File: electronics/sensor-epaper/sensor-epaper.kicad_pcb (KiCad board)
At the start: 4 copper layers, 34 x 68 mm, 74 parts, among them J1 i2c, J2 SWD, J4 Display, Q1 Q_NMOS_GSD, Q2 NX2301P, U2 ATSAMD21G18A-A, U3 AP3012, Y1 32.768

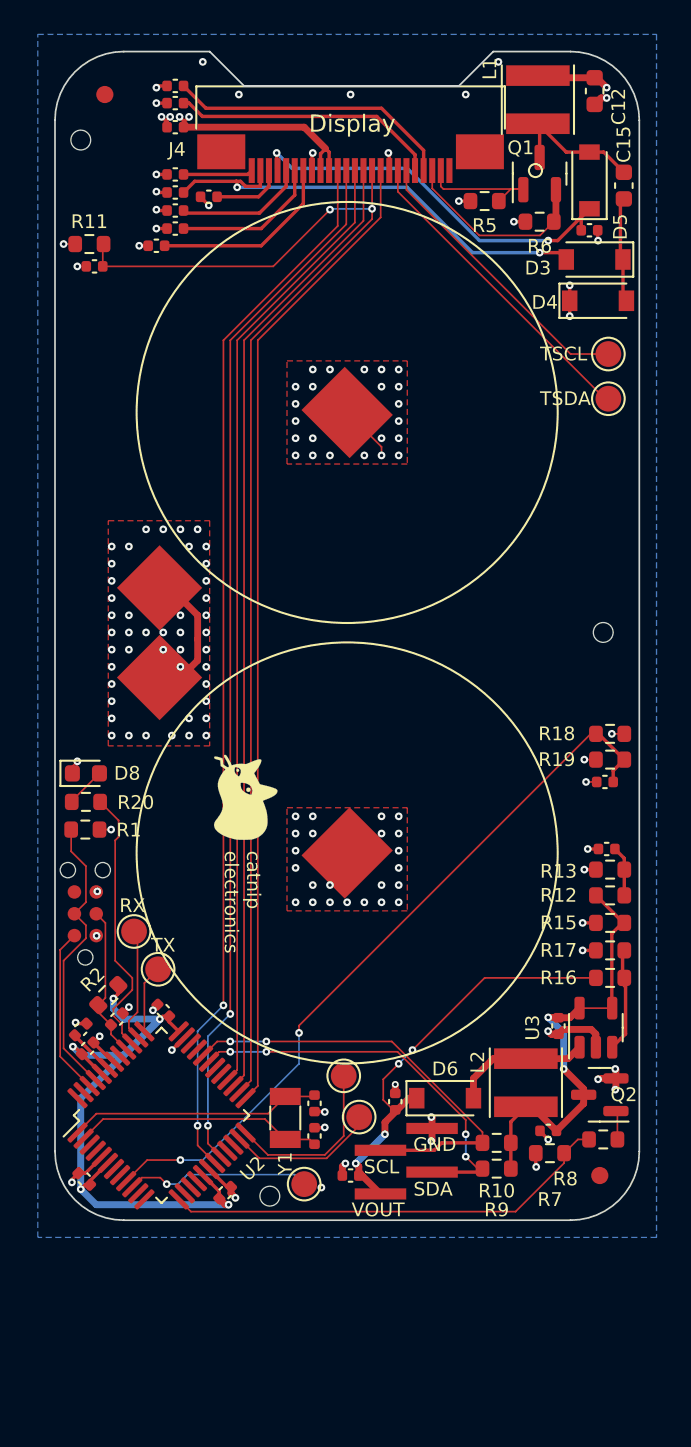
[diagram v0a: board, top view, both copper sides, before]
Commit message: Implement fixes for v1.0.0 board: * Fixed mirrored display connector * Fixed wrong button pinout * Remove CS from GPIO11 which is VDD_SPI after all, add a requisite cap * Add tantallum bulk cap, add more capacitance near MCU to counter power gulp related resets using thin USB cable * Consolidate some passive values
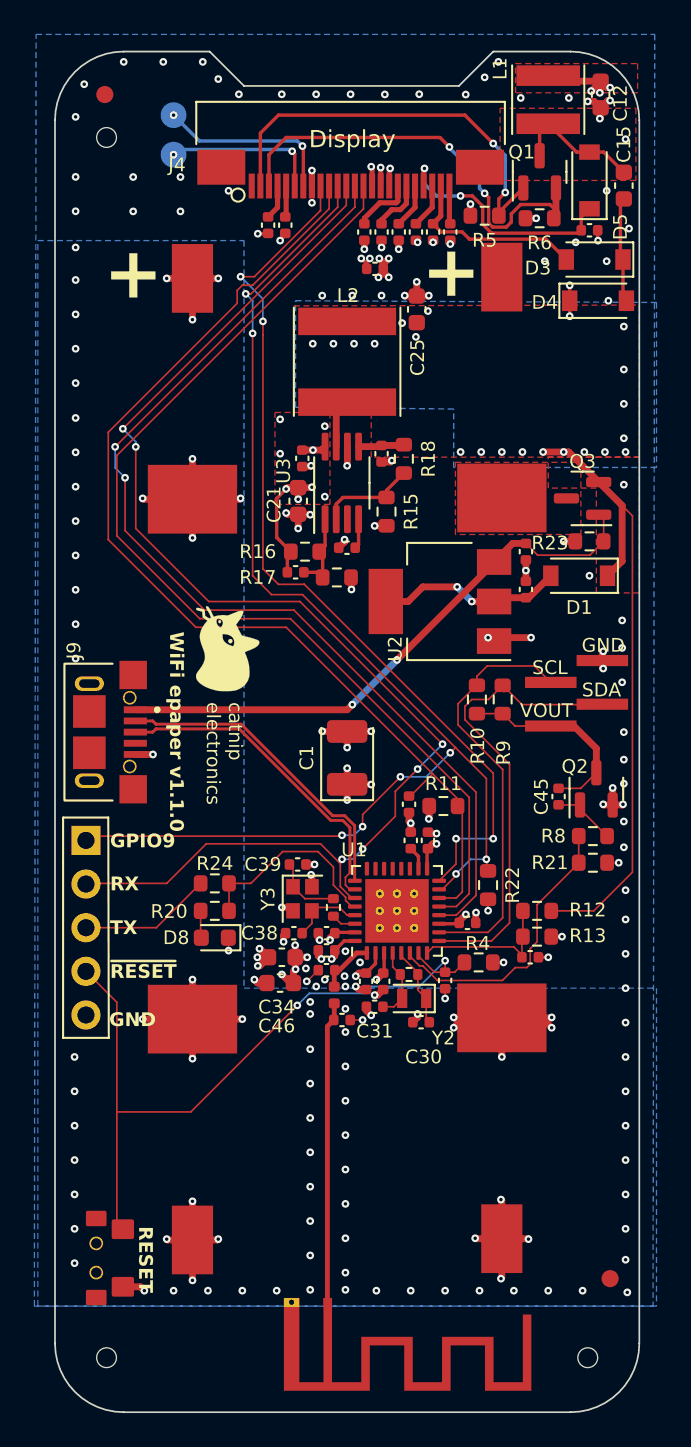
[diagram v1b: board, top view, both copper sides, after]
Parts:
- removed C19, C20, C3, C4, C5, C6: 1u, Capacitor_SMD:C_0402_1005Metric
- removed C2: 22p, Capacitor_SMD:C_0402_1005Metric
- removed D6: MBR0530, Diode_SMD:D_SOD-123
- removed the H6 at (178.5, 103.6)
- removed the H6 at (197.9, 70.8)
- removed R1, R2: 1k, Resistor_SMD:R_0603_1608Metric
- removed R19, R7: 1M, Resistor_SMD:R_0603_1608Metric
- removed TP1, TP2, TP3, TP4, TP5: TestPoint, TestPoint:TestPoint_Pad_D1.5mm
- removed Y1: 32.768, Crystal:Crystal_SMD_3215-2Pin_3.2x1.5mm
- added AE1: PCB Antenna, miceuz-lib:Texas_SWRA117D_2.4GHz_Left, F.Cu at (181.9, 109.8)
- added C28: 1u, Capacitor_SMD:C_0402_1005Metric, F.Cu at (187.7, 82.9)
- added C29: 1u, Capacitor_SMD:C_0402_1005Metric, F.Cu at (181.8, 89.3)
- added C30: 18p, Capacitor_SMD:C_0402_1005Metric, F.Cu at (187.3, 93.5)
- added C31: 18p, Capacitor_SMD:C_0402_1005Metric, F.Cu at (184.6, 92.6)
- added C32: 1u, Capacitor_SMD:C_0402_1005Metric, F.Cu at (190.0, 87.7)
- added C33: 1u, Capacitor_SMD:C_0402_1005Metric, F.Cu at (184.1, 91.1)
- added C34: 22u, Capacitor_SMD:C_0603_1608Metric, F.Cu at (179.2, 89.7)
- added C35: 1u, Capacitor_SMD:C_0402_1005Metric, F.Cu at (188.7, 91.0)
- added C36: ?, Capacitor_SMD:C_0402_1005Metric, F.Cu at (181.8, 90.5)
- added C37: ?, Capacitor_SMD:C_0402_1005Metric, F.Cu at (182.7, 93.3)
- added C38: 12p, Capacitor_SMD:C_0402_1005Metric, F.Cu at (179.9, 88.3)
- added C39: 12p, Capacitor_SMD:C_0402_1005Metric, F.Cu at (180.1, 84.3)
- added C40: 1u, Capacitor_SMD:C_0402_1005Metric, F.Cu at (185.1, 91.1)
- added C41: 1u, Capacitor_SMD:C_0402_1005Metric, F.Cu at (181.8, 88.3)
- added C42: 10p, Capacitor_SMD:C_0402_1005Metric, F.Cu at (180.0, 67.3)
- added C43: 1u, Capacitor_SMD:C_0402_1005Metric, F.Cu at (193.4, 66.1)
- added C44: 1u, Capacitor_SMD:C_0402_1005Metric, F.Cu at (193.4, 68.3)
- added C45: 1u, Capacitor_SMD:C_0402_1005Metric, F.Cu at (195.3, 80.3)
- added C46: 22u, Capacitor_SMD:C_0603_1608Metric, F.Cu at (179.1, 91.2)
- added C47: 1u, Capacitor_SMD:C_0402_1005Metric, F.Cu at (186.7, 82.9)
- added D1: 1N4148, Diode_SMD:D_SOD-123, F.Cu at (196.5, 67.5)
- added H6: ToolingHole, miceuz-lib:JLC_ToolingHole, F.Cu at (197.0, 113.0)
- added H6: ToolingHole, miceuz-lib:JLC_ToolingHole, F.Cu at (169.0, 113.0)
- added J9: USB micro, miceuz-lib:XKB_U254-051T-4BH83-F1S, F.Cu at (168.0, 76.6)
- added L3: 0, Inductor_SMD:L_0402_1005Metric, F.Cu at (182.2, 91.9)
- added Q3: NX2301P, Package_TO_SOT_SMD:SOT-23, F.Cu at (196.7, 63.0)
- added R14: 0, Resistor_SMD:R_0402_1005Metric, F.Cu at (182.2, 86.8)
- added R21: 1M, Resistor_SMD:R_0603_1608Metric, F.Cu at (197.3, 84.2)
- added R22: 1M, Resistor_SMD:R_0603_1608Metric, F.Cu at (191.2, 85.5)
- added R23: 4.7k, Resistor_SMD:R_0603_1608Metric, F.Cu at (197.1, 65.5)
- added R24: 150, Resistor_SMD:R_0603_1608Metric, F.Cu at (175.3, 85.4)
- added R3: ?, Resistor_SMD:R_0402_1005Metric, F.Cu at (186.6, 90.7)
- added R4: 4.7k, Resistor_SMD:R_0603_1608Metric, F.Cu at (190.7, 90.0)
- added SW1: SW_Push, miceuz-lib:SHOUHAN_TS24CA, F.Cu at (168.4, 107.2)
- added U1: ESP32-C3FN4, Package_DFN_QFN:QFN-32-1EP_5x5mm_P0.5mm_EP3.7x3.7mm_ThermalVias, F.Cu at (185.9, 87.0)
- added Y2: 32kHz, Crystal:Crystal_SMD_2012-2Pin_2.0x1.2mm, F.Cu at (186.9, 92.1)
- added Y3: 40MHz 10ppm, Crystal:Crystal_SMD_2016-4Pin_2.0x1.6mm, F.Cu at (180.4, 86.3)
- BT1, BT2: footprint miceuz-lib:2450_battery -> miceuz-lib:AA_KEYCO_53_SMD
- C1: value 22p -> 100u; footprint Capacitor_SMD:C_0402_1005Metric -> Capacitor_Tantalum_SMD:CP_EIA-3528-15_AVX-H
- C21, C25: value 1u -> 22u; footprint Capacitor_SMD:C_0402_1005Metric -> Capacitor_SMD:C_0603_1608Metric
- J2: value SWD -> Conn_01x06; footprint miceuz-lib:TC2030-MCP-NL -> Connector_PinHeader_2.54mm:PinHeader_1x05_P2.54mm_Vertical
- L2: footprint Inductor_SMD:L_Taiyo-Yuden_NR-40xx -> Inductor_SMD:L_Taiyo-Yuden_NR-60xx
- R11, R20: value 1k -> 4.7k
- R15: value 1k -> 300k
- R16: value 1k -> 348k
- R17: value 1k -> 200k
- R18: value 1M -> 220k
- R5: value 10k -> 4.7k
- TP6: value TSCL -> TestPoint; moved to B.Cu
- TP7: value TSDA -> TestPoint; moved to B.Cu
- U2: value ATSAMD21G18A-A -> AMS1117-3.3; footprint Package_QFP:TQFP-48_7x7mm_P0.5mm -> Package_TO_SOT_SMD:SOT-223-3_TabPin2
- U3: value AP3012 -> NCP1421; footprint Package_TO_SOT_SMD:SOT-23-5 -> Package_SO:MSOP-8_3x3mm_P0.65mm
- moved C25 48.4 mm to (187.1, 52.0), turned to 90 degrees
- moved L2 43.2 mm to (183.0, 55.0), turned to -90 degrees
- moved C22 41.8 mm to (180.4, 60.7), turned to -90 degrees
- moved R11 38.6 mm to (188.6, 80.9)
- moved C23 36.3 mm to (186.6, 80.8), turned to -90 degrees
- moved C21 35.4 mm to (180.2, 63.1), turned to -90 degrees
- moved U3 35.0 mm to (182.7, 62.1)
- moved C26 34.9 mm to (185.0, 60.4)
- moved U2 34.0 mm to (188.4, 69.0), turned to 0 degrees
- moved R16 30.5 mm to (180.6, 66.1)
- moved TP7 30.2 mm to (172.9, 40.7), turned to -90 degrees
- moved J1 29.0 mm to (196.3, 74.3)
- moved TP6 27.8 mm to (172.9, 43.0), turned to -90 degrees
- moved R9 27.3 mm to (192.1, 74.7), turned to 90 degrees
- moved R15 27.2 mm to (185.3, 63.8), turned to -90 degrees
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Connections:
- net Net-(D5-A) renamed /SW_NODE_DISPLAY
- net Net-(Q2-G) renamed /I2C-interface/I2C_EN_GATE
- BT1 pad 1: +BATT -> /MID_BATT
- BT2 pad 2: GND -> /MID_BATT
- C1 pad 1: Net-(U2-PA00) -> +3V3
- C12 pad 1: +BATT -> +3V3
- C21 pad 1: /I2C-interface/VOUT -> +3V3
- C22 pad 1: /I2C-interface/VOUT -> +3V3
- C24 pad 1: /I2C-interface/VIN_FEEDBACK -> /BATT_VOLTAGE
- C25 pad 1: Net-(Q2-D) -> /VIN
- C26 pad 1: Net-(Q2-D) -> /VIN
- C27 pad 1: /BATT_VOLTAGE -> /REF_MAIN
- C8 pad 1: +BATT -> +3V3
- J1 pad 1: /I2C-interface/VOUT -> /VI2C
- J2 pad 1: +BATT -> /D/C
- J2 pad 2: /SWD_IO -> /~{CS}
- J2 pad 3: /~{MCU_RST} -> Net-(J2-Pin_3)
- J2 pad 4: /SWD_CLK -> /CHIP_EN
- J4 pad 15: +BATT -> +3V3
- J4 pad 16: +BATT -> +3V3
- L1 pad 1: +BATT -> +3V3
- L2 pad 1: Net-(Q2-D) -> /VIN
- L2 pad 2: Net-(D6-A) -> /SW_MAIN
- Q2 pad 2: +BATT -> +3V3
- Q2 pad 3: Net-(Q2-D) -> /VI2C
- R10 pad 1: Net-(Q2-D) -> /VI2C
- R11 pad 1: +BATT -> +3V3
- R12 pad 1: Net-(Q2-D) -> /VIN
- R12 pad 2: /I2C-interface/VIN_FEEDBACK -> /BATT_VOLTAGE
- R13 pad 1: /I2C-interface/VIN_FEEDBACK -> /BATT_VOLTAGE
- R15 pad 1: Net-(Q2-D) -> /EN_MAIN
- R16 pad 1: /I2C-interface/VOUT -> +3V3
- R16 pad 2: Net-(U3-FB) -> /FB_MAIN
- R17 pad 1: Net-(U3-FB) -> /FB_MAIN
- R18 pad 1: +BATT -> /VIN
- R18 pad 2: /BATT_VOLTAGE -> /EN_MAIN
- R20 pad 2: Net-(U2-PA27) -> /TXD
- R9 pad 1: Net-(Q2-D) -> /VI2C
- U2 pad 1: Net-(U2-PA00) -> GND
- U2 pad 2: Net-(U2-PA01) -> /USB_3V3
- U2 pad 3: unconnected-(U2-PA02/A0) -> VBUS
- U3 pad 1: Net-(D6-A) -> /FB_MAIN
- U3 pad 2: GND -> /EN_MAIN
- U3 pad 3: Net-(U3-FB) -> (no net)
- U3 pad 4: Net-(Q2-D) -> /REF_MAIN
- U3 pad 5: Net-(Q2-D) -> /VIN
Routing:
- net +BATT: track 72.0 -> 0.00 mm, vias 66 -> 0
- net /CHIP_EN: track 0.00 -> 42.6 mm, vias 0 -> 2
- net /VIN: track 0.00 -> 42.0 mm, vias 0 -> 16
- net +3V3: track 0.00 -> 41.7 mm, vias 0 -> 37
- net /MID_BATT: track 0.00 -> 37.7 mm, vias 0 -> 16
- net /BATT_VOLTAGE: track 43.3 -> 8.50 mm, vias 2 -> 0
- net VBUS: track 0.00 -> 33.5 mm, vias 0 -> 2
- net Net-(Q2-D): track 25.9 -> 0.00 mm, vias 2 -> 0
- net GND: track 40.1 -> 65.9 mm, vias 88 -> 194
- net /I2C-interface/VOUT: track 25.0 -> 0.00 mm, vias 4 -> 0
- net /~{CS}: track 56.0 -> 76.7 mm, vias 0 -> 6
- net /D/C: track 56.4 -> 76.1 mm, vias 0 -> 8
- net /D+: track 0.00 -> 18.7 mm
- net /D-: track 0.00 -> 18.5 mm
- net /ANT_COMP: track 0.00 -> 17.5 mm
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- added copper zone on B.Cu, net +3V3
- added copper zone on F.Cu, net +3V3
- added copper zone on B.Cu, net /MID_BATT
- added copper zone on F.Cu, net /SW_NODE_DISPLAY
- added copper zone on B.Cu, net /VIN
- added copper zone on F.Cu, net /VIN
- removed copper zone on B.Cu, net +BATT
- removed copper zone on F.Cu, net GND
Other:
- board size 34 x 68 mm -> 34 x 79.2 mm
- board text added: "0,0900 mm / 0,0900 mm"
- board text added: "0,2000 mm"
- board text added: "0,7800 mm"
- board text added: "34,0000 mm x 79,1716 mm"
- board text added: "4"
- board text added: "AA battery dimensions: 50.5x14.5mm"
- board text added: "BOARD CHARACTERISTICS"
- board text added: "Board Thickness:"
- board text added: "Board overall dimensions:"
- board text added: "Castellated pads:"
- board text added: "Copper Finish:"
- board text added: "Copper Layer Count:"
- board text added: "Edge card connectors:"
- board text added: "GPIO9"
- board text added: "Impedance Control:"
- board text added: "Min hole diameter:"
- board text added: "Min track/spacing:"
- board text added: "No"
- board text added: "None"
- board text added: "Plated Board Edge:"
- board text added: "RESET"
- board text added: "WiFi epaper v1.1.0"
- board text added: "~{RESET}"

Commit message: Shuffle stuff on User Comments layer, hunt kicad format changes
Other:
- board text added: "0,0858 mm / 0,0900 mm"
- board text added: "1,6000 mm"
- board text removed: "0,0900 mm / 0,0900 mm"
- board text removed: "0,7800 mm"
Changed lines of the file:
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@@
 (kicad_pcb (version 20221018) (generator pcbnew)
   (general
-    (thickness 0.799999)
+    (thickness 1.6)
   )
   (paper "A4")
@@
       (layer "F.Mask" (type "Top Solder Mask") (thickness 0.01))
       (layer "F.Cu" (type "copper") (thickness 0.035))
-      (layer "dielectric 1" (type "core") (thickness 0.213333) (material "FR4") (epsilon_r 4.5) (loss_tangent 0.02))
+      (layer "dielectric 1" (type "prepreg") (thickness 0.1) (material "FR4") (epsilon_r 4.5) (loss_tangent 0.02))
       (layer "In1.Cu" (type "copper") (thickness 0.035))
-      (layer "dielectric 2" (type "prepreg") (thickness 0.213333) (material "FR4") (epsilon_r 4.5) (loss_tangent 0.02))
+      (layer "dielectric 2" (type "core") (thickness 1.24) (material "FR4") (epsilon_r 4.5) (loss_tangent 0.02))
       (layer "In2.Cu" (type "copper") (thickness 0.035))
-      (layer "dielectric 3" (type "core") (thickness 0.213333) (material "FR4") (epsilon_r 4.5) (loss_tangent 0.02))
+      (layer "dielectric 3" (type "prepreg") (thickness 0.1) (material "FR4") (epsilon_r 4.5) (loss_tangent 0.02))
       (layer "B.Cu" (type "copper") (thickness 0.035))
       (layer "B.Mask" (type "Bottom Solder Mask") (thickness 0.01))
@@
     (effects (font (size 0.8 0.8) (thickness 0.15)))
   )
-  (gr_text "34,0000 mm x 79,1716 mm" (at 209.75 148) (layer "Cmts.User")
-    (effects (font (size 1.5 1.5) (thickness 0.2)) (justify left top))
+  (gr_text "BOARD CHARACTERISTICS" (at 171 134.6) (layer "Cmts.User")
+    (effects (font (size 2 2) (thickness 0.4)) (justify left top))
   )
-  (gr_text "No" (at 209.75 161.2) (layer "Cmts.User")
+  (gr_text "Plated Board Edge: " (at 236.264282 152.15) (layer "Cmts.User")
     (effects (font (size 1.5 1.5) (thickness 0.2)) (justify left top))
   )
-  (gr_text "Plated Board Edge: " (at 242.63571 157.9) (layer "Cmts.User")
+  (gr_text "Castellated pads: " (at 171.75 152.15) (layer "Cmts.User")
     (effects (font (size 1.5 1.5) (thickness 0.2)) (justify left top))
   )
-  (gr_text "No" (at 266.792853 154.6) (layer "Cmts.User")
+  (gr_text "34,0000 mm x 79,1716 mm" (at 203.378572 142.25) (layer "Cmts.User")
     (effects (font (size 1.5 1.5) (thickness 0.2)) (justify left top))
   )
-  (gr_text "Min hole diameter: " (at 242.63571 151.3) (layer "Cmts.User")
+  (gr_text "Edge card connectors: " (at 171.75 155.45) (layer "Cmts.User")
     (effects (font (size 1.5 1.5) (thickness 0.2)) (justify left top))
   )
-  (gr_text "Copper Layer Count: " (at 178.121428 144.7) (layer "Cmts.User")
+  (gr_text "No" (at 260.421425 152.15) (layer "Cmts.User")
     (effects (font (size 1.5 1.5) (thickness 0.2)) (justify left top))
   )
-  (gr_text "" (at 266.792853 148) (layer "Cmts.User")
+  (gr_text "Copper Finish: " (at 171.75 148.85) (layer "Cmts.User")
     (effects (font (size 1.5 1.5) (thickness 0.2)) (justify left top))
   )
-  (gr_text "No" (at 266.792853 157.9) (layer "Cmts.User")
+  (gr_text "No" (at 260.421425 148.85) (layer "Cmts.User")
     (effects (font (size 1.5 1.5) (thickness 0.2)) (justify left top))
   )
-  (gr_text "0,2000 mm" (at 266.792853 151.3) (layer "Cmts.User")
+  (gr_text "" (at 260.421425 142.25) (layer "Cmts.User")
     (effects (font (size 1.5 1.5) (thickness 0.2)) (justify left top))
   )
-  (gr_text "Impedance Control: " (at 242.63571 154.6) (layer "Cmts.User")
+  (gr_text "No" (at 203.378572 155.45) (layer "Cmts.User")
     (effects (font (size 1.5 1.5) (thickness 0.2)) (justify left top))
   )
-  (gr_text "Board Thickness: " (at 242.63571 144.7) (layer "Cmts.User")
+  (gr_text "Board Thickness: " (at 236.264282 138.95) (layer "Cmts.User")
     (effects (font (size 1.5 1.5) (thickness 0.2)) (justify left top))
   )
-  (gr_text "No" (at 209.75 157.9) (layer "Cmts.User")
+  (gr_text "0,0858 mm / 0,0900 mm" (at 203.378572 145.55) (layer "Cmts.User")
     (effects (font (size 1.5 1.5) (thickness 0.2)) (justify left top))
   )
-  (gr_text "BOARD CHARACTERISTICS" (at 177.371428 140.35) (layer "Cmts.User")
-    (effects (font (size 2 2) (thickness 0.4)) (justify left top))
-  )
-  (gr_text "Min track/spacing: " (at 178.121428 151.3) (layer "Cmts.User")
+  (gr_text "1,6000 mm" (at 260.421425 138.95) (layer "Cmts.User")
     (effects (font (size 1.5 1.5) (thickness 0.2)) (justify left top))
   )
-  (gr_text "0,0900 mm / 0,0900 mm" (at 209.75 151.3) (layer "Cmts.User")
+  (gr_text "0,2000 mm" (at 260.421425 145.55) (layer "Cmts.User")
     (effects (font (size 1.5 1.5) (thickness 0.2)) (justify left top))
   )
-  (gr_text "Copper Finish: " (at 178.121428 154.6) (layer "Cmts.User")
+  (gr_text "No" (at 203.378572 152.15) (layer "Cmts.User")
     (effects (font (size 1.5 1.5) (thickness 0.2)) (justify left top))
   )
-  (gr_text "Edge card connectors: " (at 178.121428 161.2) (layer "Cmts.User")
+  (gr_text "4" (at 203.378572 138.95) (layer "Cmts.User")
     (effects (font (size 1.5 1.5) (thickness 0.2)) (justify left top))
   )
-  (gr_text "None" (at 209.75 154.6) (layer "Cmts.User")
+  (gr_text "None" (at 203.378572 148.85) (layer "Cmts.User")
     (effects (font (size 1.5 1.5) (thickness 0.2)) (justify left top))
   )
-  (gr_text "Castellated pads: " (at 178.121428 157.9) (layer "Cmts.User")
+  (gr_text "Copper Layer Count: " (at 171.75 138.95) (layer "Cmts.User")
     (effects (font (size 1.5 1.5) (thickness 0.2)) (justify left top))
   )
-  (gr_text "Board overall dimensions: " (at 178.121428 148) (layer "Cmts.User")
+  (gr_text "AA battery dimensions: 50.5x14.5mm" (at 166 125.8) (layer "Cmts.User")
+    (effects (font (size 0.8 0.8) (thickness 0.15) bold) (justify left bottom))
+  )
+  (gr_text "Impedance Control: " (at 236.264282 148.85) (layer "Cmts.User")
     (effects (font (size 1.5 1.5) (thickness 0.2)) (justify left top))
   )
-  (gr_text "AA battery dimensions: 50.5x14.5mm" (at 165.65 116.35) (layer "Cmts.User")
-    (effects (font (size 0.8 0.8) (thickness 0.15) bold) (justify left bottom))
+  (gr_text "Min hole diameter: " (at 236.264282 145.55) (layer "Cmts.User")
+    (effects (font (size 1.5 1.5) (thickness 0.2)) (justify left top))
   )
-  (gr_text "" (at 242.63571 148) (layer "Cmts.User")
+  (gr_text "Board overall dimensions: " (at 171.75 142.25) (layer "Cmts.User")
     (effects (font (size 1.5 1.5) (thickness 0.2)) (justify left top))
   )
-  (gr_text "4" (at 209.75 144.7) (layer "Cmts.User")
+  (gr_text "" (at 236.264282 142.25) (layer "Cmts.User")
     (effects (font (size 1.5 1.5) (thickness 0.2)) (justify left top))
   )
-  (gr_text "0,7800 mm" (at 266.792853 144.7) (layer "Cmts.User")
+  (gr_text "Min track/spacing: " (at 171.75 145.55) (layer "Cmts.User")
     (effects (font (size 1.5 1.5) (thickness 0.2)) (justify left top))
   )
@@
   )
   (dimension (type aligned) (layer "Cmts.User")
-    (pts (xy 200 101) (xy 166 101))
+    (pts (xy 200 110.5) (xy 166 110.5))
     (height -10)
-    (gr_text "34.0000 mm" (at 183 110.05) (layer "Cmts.User")
+    (gr_text "34,0000 mm" (at 183 119.55) (layer "Cmts.User")
       (effects (font (size 0.8 0.8) (thickness 0.15)))
     )
@@
   )
   (dimension (type aligned) (layer "Cmts.User")
-    (pts (xy 196 105) (xy 196 37))
+    (pts (xy 196 116.171573) (xy 196 37))
     (height 13)
-    (gr_text "68.0000 mm" (at 208.05 71 90) (layer "Cmts.User")
+    (gr_text "79.1716 mm" (at 208.05 76.585787 90) (layer "Cmts.User")
       (effects (font (size 0.8 0.8) (thickness 0.15)))
     )
@@
     )
   )
-  (group "group-boardCharacteristics" (id ecf53456-9700-4f7b-ae45-8f83820d9ff2)
+  (group "group-boardCharacteristics" (id e504bf7e-bd1b-4790-9118-a65027918921)
     (members
-      09803bfb-ad00-4b54-9ba7-0483b6e573aa
-      1198f4a1-2f5b-4ca1-9a3d-bf90195eed9a
-      17da6250-036d-4895-a29e-e5ab2226302d
-      18c042a4-7226-43a3-93dc-48cbd7cbf0e2
-      2c72e6ff-cbfe-4f38-93d5-43a1e9772f1a
-      30b42dba-907f-43a5-af12-768def15ae57
-      321df59d-e39d-476b-8b9e-f5d86a630207
-      3a9cf157-2897-4fb0-a2f4-061c311d4260
-      3e76db8a-4d1e-43a1-bb0d-8195d2ecf692
-      487cdada-f8cf-4a9a-aaef-5bdc3f3c52c1
-      52daa596-e905-474a-84ad-704d12a070e2
-      6a0e3b71-b84c-4a8b-926f-8f5ddeadc207
-      7ed8e47a-a68a-471e-9750-5fa7141e2c60
-      8d0304fc-a738-42e8-bf19-7cacb960f329
-      9ae65a00-f69a-435c-ae6d-e25e86ccf920
-      9c5429ee-0fcc-4b0b-9aac-fa75aaa0882f
-      a369c465-b32b-4ff6-80b7-6175aec55f25
-      a87911cc-b486-46f5-83ca-968f8ef407f2
-      b0b3cbb7-cc8f-42e2-8633-82523c9c3a60
-      b2e92c05-98aa-4e31-ad01-22d20428239e
-      e34d1296-a3f4-4edc-a45f-710833986077
-      ed75ed28-6fd1-41a5-928b-334bdd52e68b
-      f6581851-dc95-4b99-a077-47742d339f58
+      02ee5c24-b53e-437f-87c1-98f2c13329a8
+      09d8fa25-8921-4666-9bf9-db7bed1c7b33
+      0d9381a5-6e91-43f9-b114-cf4e8ae207cc
+      0fb4fcc7-7971-471f-a786-a6fba577a9df
+      14cd226d-a079-459c-9aaf-cab3ff194d49
+      2d76b0a3-5b7b-45d4-b3b6-8e1e85e2ff86
+      381d14e4-5430-40df-afdd-57a7fa1bb05b
+      38f015f2-20f6-4cc9-afad-5354ce706b4f
+      53bf74ce-a57a-43af-a462-693a322ca7fa
+      576dbf72-c46c-4093-9dc2-08224e305c88
+      5be8715d-b35f-497a-9f92-0983c0705eac
+      5fe89346-e6fc-4793-8cbd-38eae9cfadbb
+      6b0b0457-feca-4020-a117-baed7544eaf5
+      9af96400-1b9f-4978-a275-20847f1b5708
+      a9ba68cc-4c3b-4dbd-bdcc-421fabb37d1e
+      c711e8df-7bd3-4fe5-b833-ad5bcc5bf5fd
+      cff60cbe-a7f2-4ff3-9e54-09b0d4a25a72
+      d2517a23-103b-4889-8ba7-8daa8d38814b
+      efe73271-b167-4697-81c8-a7ba704f8170
+      efec23cb-62b2-4a73-a77a-25d1cdeb86ab
+      f4423016-6145-4f30-8673-5aee3520531c
+      fcf0f771-d660-4b65-8e0d-3836cba69219
+      ff1d6f47-ef96-49b0-9086-55338ae4ec77
     )
   )
